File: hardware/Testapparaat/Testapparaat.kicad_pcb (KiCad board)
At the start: 2 copper layers, 102 parts, among them J1 MEM2051-00-195-00-A, J10 B-, J11 Display_shield, J2 Module_1, J3 Module_2, J4 DEBUG, J5 FPC_40P_LCD_ILI9488, J6 DB9_Female, J7 Emergency Stop Button, J8 CON-SOCJ-2155, J9 B+, Q1 BC817, Q2 BC817, Q3 BC817, Q4 IRFR9024N, Q5 IRFR9024N, Q6 IRFR9024N, SW1 RST, SW2 on/off switch, SW3 Menu, SW4 Back, SW5 RotaryEncoder_Switch, SW6 START, SW7 STOP, U1 74HC595 (SIPO Shift register), U2 ESP32-WROOM-32, U3 MAX232, U4 74AUC1G74, U5 TCA9534 (IO Expander), U6 74HC14

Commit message: -enh Made a start at pcb design
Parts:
- removed C6: 2.2u, Capacitor_SMD:C_0603_1608Metric_Pad1.08x0.95mm_HandSolder
- removed D8: 1N5401, Diode_THT:D_DO-201AD_P15.24mm_Horizontal
- removed D9: 1N4448, Diode_THT:D_DO-35_SOD27_P7.62mm_Horizontal
- removed PS1, PS2: LMR50410YFQDBVRQ1, LMR50410YFQDBVRQ1:SOT95P280X145-6N
- removed SW3: Menu, Button_Switch_SMD:SW_SPST_B3S-1000
- removed SW4: Back, Button_Switch_SMD:SW_SPST_B3S-1000
- removed SW5: RotaryEncoder_Switch, Rotary_Encoder:RotaryEncoder_Alps_EC11E-Switch_Vertical_H20mm_CircularMountingHoles
- removed SW6: START, Button_Switch_SMD:SW_SPST_B3S-1000
- removed SW7: STOP, Button_Switch_SMD:SW_SPST_B3S-1000
- removed U3: MAX232, Package_SO:SO-16_3.9x9.9mm_P1.27mm
- added C22: 100n, Capacitor_SMD:C_0603_1608Metric_Pad1.08x0.95mm_HandSolder, F.Cu at (71.8, 101.8)
- added J12: GPIO_INPUTS, Connector_PinHeader_2.54mm:PinHeader_1x04_P2.54mm_Horizontal, F.Cu at (99.4, -21.1)
- added J13: FrontPanel, Connector_PinHeader_2.54mm:PinHeader_2x08_P2.54mm_Vertical_SMD, F.Cu at (159.9, -9.95)
- added J14: GPIO_OUTPUT, Connector_PinHeader_2.54mm:PinHeader_2x04_P2.54mm_Vertical_SMD, F.Cu at (69.3, 6.75)
- added R38: 10k, Resistor_SMD:R_0603_1608Metric_Pad0.98x0.95mm_HandSolder, F.Cu at (123.5, -3.29)
- added R40: 10k, Resistor_SMD:R_0603_1608Metric_Pad0.98x0.95mm_HandSolder, F.Cu at (111.6, -3.85)
- added R41: 10k, Resistor_SMD:R_0603_1608Metric_Pad0.98x0.95mm_HandSolder, F.Cu at (112.5, 0.90)
- added R42: 10k, Resistor_SMD:R_0603_1608Metric_Pad0.98x0.95mm_HandSolder, F.Cu at (168.8, -3.05)
- added R43: 10k, Resistor_SMD:R_0603_1608Metric_Pad0.98x0.95mm_HandSolder, F.Cu at (174.2, -9.40)
- added R44: 10k, Resistor_SMD:R_0603_1608Metric_Pad0.98x0.95mm_HandSolder, F.Cu at (167.9, 2.10)
- added U10: LM2596S-5, Package_TO_SOT_SMD:TO-263-5_TabPin3, F.Cu at (179.3, 137.6)
- added U11: LM2596S-3.3, Package_TO_SOT_SMD:TO-263-5_TabPin3, F.Cu at (197.0, 137.6)
- added U12: 74AUC1G74, Package_SO:VSSOP-8_2.3x2mm_P0.5mm, F.Cu at (98.2, -11.9)
- added U7: TCA9534 (IO Expander), TCA9534:SOP65P640X120-16N, F.Cu at (106.7, 2.20)
- added U8: 74HC14, Package_SO:SO-14_3.9x8.65mm_P1.27mm, F.Cu at (120.7, -14.4)
- added U9: 74HC14, Package_SO:SO-14_3.9x8.65mm_P1.27mm, F.Cu at (107.0, -14.7)
- C1, J4, Q1, Q2, R4, R5: moved to B.Cu
- C10, C11, C12, C13: value 0.1u -> 100n
- C14, C15, C16, C17, C18, C19, C20: value 1u -> 100n
- C4, C5: value 100n -> 1u
- C7: value 2.2u -> 1u
- C8, C9: value 10u -> 220u; footprint Capacitor_SMD:C_0603_1608Metric_Pad1.08x0.95mm_HandSolder -> Capacitor_THT:C_Radial_D10.0mm_H12.5mm_P5.00mm
- D1, D2, D4: value 1N4448 -> SS310; footprint Diode_THT:D_DO-35_SOD27_P7.62mm_Horizontal -> Diode_SMD:D_SMA_Handsoldering
- D3, D5, D6, D7: value 1N4448 -> 1N4448WS; footprint Diode_THT:D_DO-35_SOD27_P7.62mm_Horizontal -> Diode_SMD:D_SOD-323
- J1: value MEM2051-00-195-00-A -> IO_SD; footprint MEM2051:MEM20510019500A -> Connector_PinHeader_2.54mm:PinHeader_1x06_P2.54mm_Horizontal
- J6: value DB9_Female -> IO_UART; footprint G17C0900132EU:G17C0900132EU -> Connector_PinHeader_2.54mm:PinHeader_1x04_P2.54mm_Horizontal
- L1: value 4.7uH -> 68uH
- L2: value 3.3uH -> 68uH
- R1: value 10k -> 1k
- R10: value 20k -> 1k
- R14, R15, R16, R17, R18, R2, R21, R22, R23, R24, R25, R26, R27, R28, R29, R34, R35: value 10k -> 22k
- R36, R37: value 10k -> 100k
- R7: value 91k -> 680
- R8: value 22k -> 220
- R9: value 43k -> 1,6k
- U4: value 74AUC1G74 -> 74HC595 (SIPO Shift register); footprint Package_SO:VSSOP-8_2.3x2mm_P0.5mm -> 74HC595D-Q100,118:74HC595DQ100118
- moved J3 166.4 mm to (253.8, 94.5)
- moved J6 160.1 mm to (58.3, 54.0), turned to 180 degrees
- moved R12 155.0 mm to (74.4, 108.5), turned to 180 degrees
- moved J11 152.6 mm to (63.6, 115.3)
- moved C4 152.4 mm to (101.4, -12.8), turned to -90 degrees
- moved R11 151.0 mm to (74.4, 109.9), turned to 180 degrees
- moved J5 149.4 mm to (90.2, 114.8), turned to 90 degrees
- moved J8 145.9 mm to (60.6, 160.7)
- moved J2 138.9 mm to (253.4, 47.5)
- moved R13 135.1 mm to (74.4, 107.0), turned to 180 degrees
- moved C13 134.6 mm to (63.9, 86.0), turned to 180 degrees
- moved J7 129.1 mm to (257.1, 20.0)
- moved R37 125.3 mm to (67.8, 87.5)
- moved C11 123.4 mm to (113.5, -7.95)
- moved SW2 122.2 mm to (65.2, 177.1), turned to 90 degrees
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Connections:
- C10 pad 1: Net-(C10-Pad1) -> +3.3V
- C10 pad 2: Net-(C10-Pad2) -> GND
- C11 pad 1: Net-(C11-Pad1) -> +3.3V
- C11 pad 2: Net-(C11-Pad2) -> GND
- C12 pad 1: GND -> +3.3V
- C12 pad 2: Net-(C12-Pad2) -> GND
- C13 pad 1: Net-(C13-Pad1) -> +3.3V
- C14 pad 1: MENU_BTN -> +3.3V
- C15 pad 1: BACK_BTN -> +3.3V
- C16 pad 1: Net-(C16-Pad1) -> +3.3V
- C17 pad 1: Net-(C17-Pad1) -> +3.3V
- C18 pad 1: Net-(C18-Pad1) -> GND
- C18 pad 2: GND -> +3.3V
- C19 pad 1: Net-(C19-Pad1) -> GND
- C19 pad 2: GND -> +3.3V
- C20 pad 1: Net-(C20-Pad1) -> +3.3V
- C4 pad 1: Net-(C4-Pad1) -> Net-(R35-Pad2)
- C4 pad 2: Net-(C4-Pad2) -> GND
- C5 pad 1: Net-(C5-Pad1) -> Net-(R29-Pad2)
- C5 pad 2: Net-(C5-Pad2) -> GND
- C7 pad 1: +BATT -> Net-(R34-Pad2)
- D1 pad 1: MENU_BTN -> Net-(D1-Pad1)
- D1 pad 2: Net-(D1-Pad2) -> GND
- D2 pad 1: BACK_BTN -> Net-(D2-Pad1)
- D2 pad 2: Net-(D2-Pad2) -> GND
- D3 pad 1: Net-(C16-Pad1) -> Net-(C21-Pad1)
- D3 pad 2: Net-(D3-Pad2) -> EMERGENCY_STOP_BTN
- D4 pad 1: Net-(C17-Pad1) -> +BATT
- D5 pad 1: Net-(C20-Pad1) -> Net-(R35-Pad2)
- D5 pad 2: Net-(D5-Pad2) -> Rotary_B_R
- D6 pad 1: Net-(C18-Pad1) -> Net-(R29-Pad2)
- D6 pad 2: Net-(D6-Pad2) -> Rotary_CLK_R
- D7 pad 1: Net-(C19-Pad1) -> Net-(R34-Pad2)
- D7 pad 2: Net-(D7-Pad2) -> Rotary_BTN_R
- J4 pad 5: /IO_port/TXD -> /MCU/GPIO_1/TXD0
- J4 pad 7: /IO_port/RXD -> /MCU/GPIO_3/RXD0
- J4 pad 9: DTS -> DTR
- J6 pad 1: unconnected-(J6-Pad1) -> +3.3V
- J6 pad 2: Net-(J6-Pad2) -> /MCU/GPIO_1/TXD0
- J6 pad 3: Net-(J6-Pad3) -> /MCU/GPIO_3/RXD0
- J6 pad 4: Net-(J6-Pad4) -> GND
- J7 pad 1: unconnected-(J7-Pad1) -> GND
- J7 pad 2: GND -> unconnected-(J7-Pad2)
- J8 pad 1: Net-(D8-Pad2) -> Net-(D4-Pad2)
- L1 pad 1: Net-(C4-Pad1) -> Net-(D1-Pad1)
- L2 pad 1: Net-(C5-Pad1) -> Net-(D2-Pad1)
- R1 pad 1: Net-(R1-Pad1) -> +3.3V
- R1 pad 2: +3.3V -> Net-(R1-Pad2)
- R14 pad 1: Net-(D1-Pad2) -> +3.3V
- R14 pad 2: GND -> BTN_4_R
- R15 pad 1: Net-(D2-Pad2) -> +3.3V
- R15 pad 2: GND -> BTN_5_R
- R16 pad 2: Net-(D5-Pad2) -> BTN_1_R
- R17 pad 2: Net-(D7-Pad2) -> BTN_2_R
- R18 pad 2: Net-(D6-Pad2) -> BTN_9_R
- R2 pad 2: Net-(R2-Pad2) -> BTN_3_R
- R21 pad 1: Net-(R21-Pad1) -> +3.3V
- R21 pad 2: +3.3V -> BTN_8_R
- R22 pad 1: Net-(D1-Pad2) -> +3.3V
- R22 pad 2: MENU_BTN -> BTN_10_R
- R23 pad 1: Net-(D2-Pad2) -> +3.3V
- R23 pad 2: BACK_BTN -> BTN_6_R
- R24 pad 1: Net-(D3-Pad2) -> +3.3V
- R24 pad 2: Net-(C16-Pad1) -> BTN_7_R
- R25 pad 1: Net-(D4-Pad2) -> +3.3V
- R25 pad 2: Net-(C17-Pad1) -> Net-(R25-Pad2)
- R26 pad 1: Net-(D4-Pad2) -> +3.3V
- R26 pad 2: +3.3V -> GPIO_INPUT_1_R
- R27 pad 1: Net-(C20-Pad1) -> +3.3V
- R27 pad 2: Net-(D5-Pad2) -> GPIO_INPUT_2_R
- R28 pad 1: Net-(D6-Pad2) -> +3.3V
- R28 pad 2: Net-(C18-Pad1) -> Net-(R28-Pad2)
- R29 pad 1: Net-(D7-Pad2) -> +3.3V
- R29 pad 2: Net-(C19-Pad1) -> Net-(R29-Pad2)
- R34 pad 2: SPI_CLK -> Net-(R34-Pad2)
- R35 pad 2: SPI_MOSI -> Net-(R35-Pad2)
- R36 pad 1: +3.3V -> /MCU/SENSOR_VN/GPIO_IN_39
- R36 pad 2: SD_CS -> ID_MOD_2
- R37 pad 1: +3.3V -> /MCU/SENSOR_VP/GPIO_IN_36
- R37 pad 2: SPI_MISO -> ID_MOD_1
- U1 pad 13: GND -> OE
- U1 pad 9: unconnected-(U1-Pad9) -> Net-(U1-Pad9)
- U2 pad 10: IO_EXP_INT -> OE
- U2 pad 11: Rotary_CLK -> RCLK
- U2 pad 12: Rotary_DT -> SRCLK
- U2 pad 34: /IO_port/RXD -> /MCU/GPIO_3/RXD0
- U2 pad 35: /IO_port/TXD -> /MCU/GPIO_1/TXD0
- U2 pad 4: ID_MOD_2 -> /MCU/SENSOR_VP/GPIO_IN_36
- U2 pad 5: ID_MOD_1 -> /MCU/SENSOR_VN/GPIO_IN_39
- U2 pad 6: SRCLK -> Rotary_DT
- U2 pad 7: SER -> IO_EXP_INT
- U2 pad 8: EMERGENCY_STOP_BTN -> SER
- U2 pad 9: RCLK -> Rotary_CLK
- U4 pad 1: Rotary_CLK -> GPIO_OUTPUT_2
- U4 pad 2: Rotary_B -> GPIO_OUTPUT_3
- U4 pad 3: unconnected-(U4-Pad3) -> GPIO_OUTPUT_4
- U4 pad 4: GND -> GPIO_OUTPUT_5
- U4 pad 5: Rotary_DT -> GPIO_OUTPUT_6
- U4 pad 6: +3.3V -> GPIO_OUTPUT_7
- U4 pad 7: +3.3V -> GPIO_OUTPUT_8
- U4 pad 8: +3.3V -> GND
- U5 pad 10: BACK_BTN -> BTN_2
- U5 pad 11: ENCODER_BTN -> BTN_3
- U5 pad 12: MOD_PSU_EN -> BTN_4
- U5 pad 6: START_BTN -> EMERGENCY_STOP_BTN
- U5 pad 7: STOP_BTN -> Rotary_BTN
- U5 pad 9: MENU_BTN -> BTN_1
- U6 pad 10: STOP_BTN -> BTN_4
- U6 pad 11: Net-(C19-Pad1) -> BTN_4_R
- U6 pad 12: ENCODER_BTN -> BTN_5
- U6 pad 13: Net-(C20-Pad1) -> BTN_5_R
- U6 pad 3: Net-(C17-Pad1) -> BTN_1_R
- U6 pad 4: Rotary_B -> BTN_1
- U6 pad 5: Net-(C16-Pad1) -> BTN_2_R
- U6 pad 6: Rotary_CLK -> BTN_2
- U6 pad 8: START_BTN -> BTN_3
- U6 pad 9: Net-(C18-Pad1) -> BTN_3_R

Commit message: -add Layout zo goed als af
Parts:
- C12, C13, C2, C3, C8, C9, D1, D2, J6, L1, L2, R10, R3, R36, R37, R6, R7, R8, R9, SW1, U10, U11, U2: moved to B.Cu
- moved J12 194.9 mm to (220.5, 131.6), turned to -90 degrees
- moved U1 194.5 mm to (239.8, 106.2)
- moved C15 192.2 mm to (247.8, 78.6)
- moved R1 192.2 mm to (240.0, 78.3)
- moved U4 192.2 mm to (237.7, 84.9)
- moved C16 192.2 mm to (234.2, 77.7)
- moved J14 190.5 mm to (238.1, 95.0)
- moved R20 184.6 mm to (230.6, 100.6), turned to -90 degrees
- moved R34 181.9 mm to (214.9, 124.0)
- moved C11 181.4 mm to (233.4, 128.3)
- moved R18 181.4 mm to (246.4, 124.3)
- moved R23 181.4 mm to (238.4, 114.8)
- moved R25 181.4 mm to (246.4, 118.4)
- moved R26 181.4 mm to (233.4, 124.1)
- moved R27 181.4 mm to (233.0, 121.7)
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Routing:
- net Net-(Q3-Pad1): track 0.00 -> 4.76 mm
- net GND: track 0.00 -> 4.76 mm
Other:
- board outline added: 141.6 x 97.8 mm

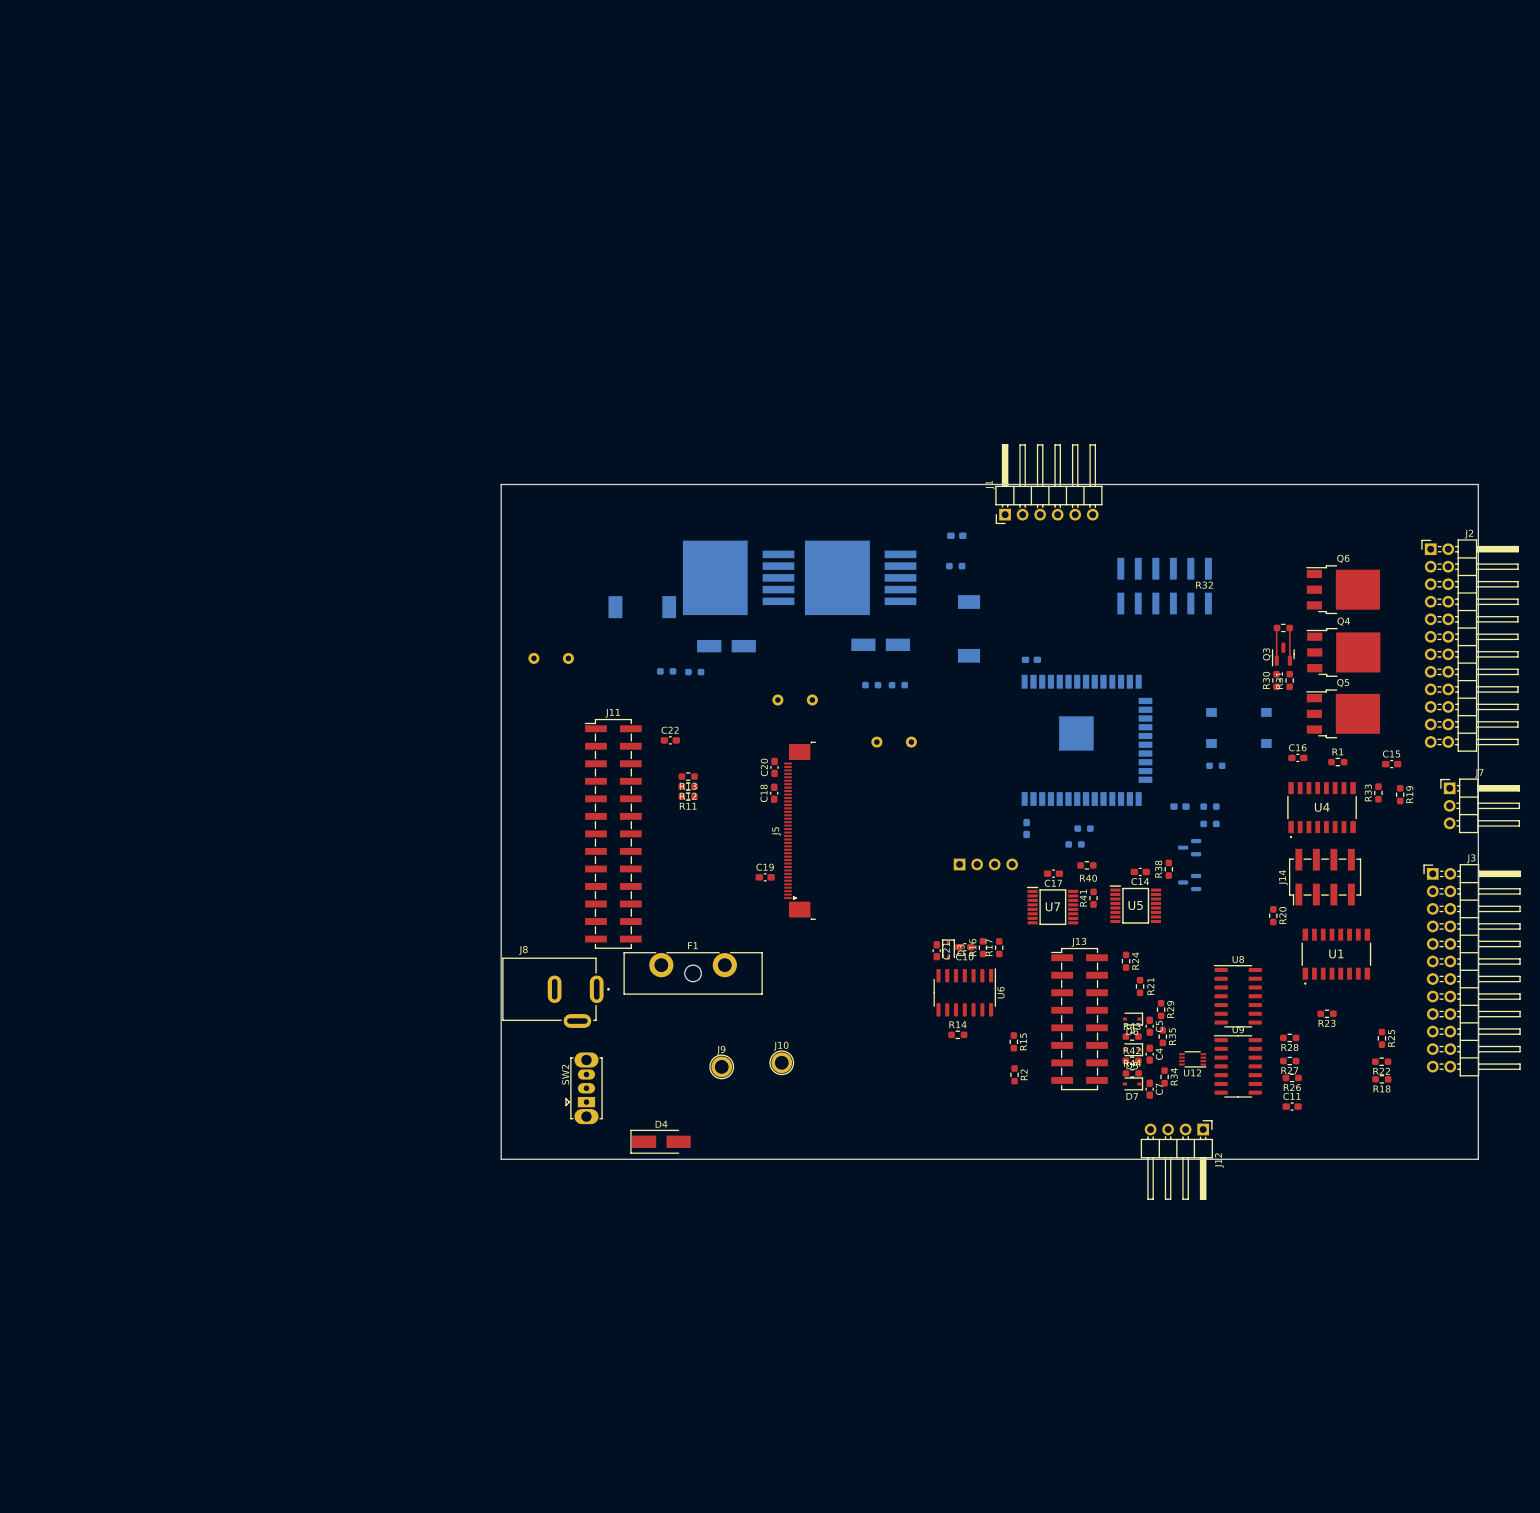
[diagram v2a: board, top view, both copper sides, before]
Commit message: -enh PCB routed power section
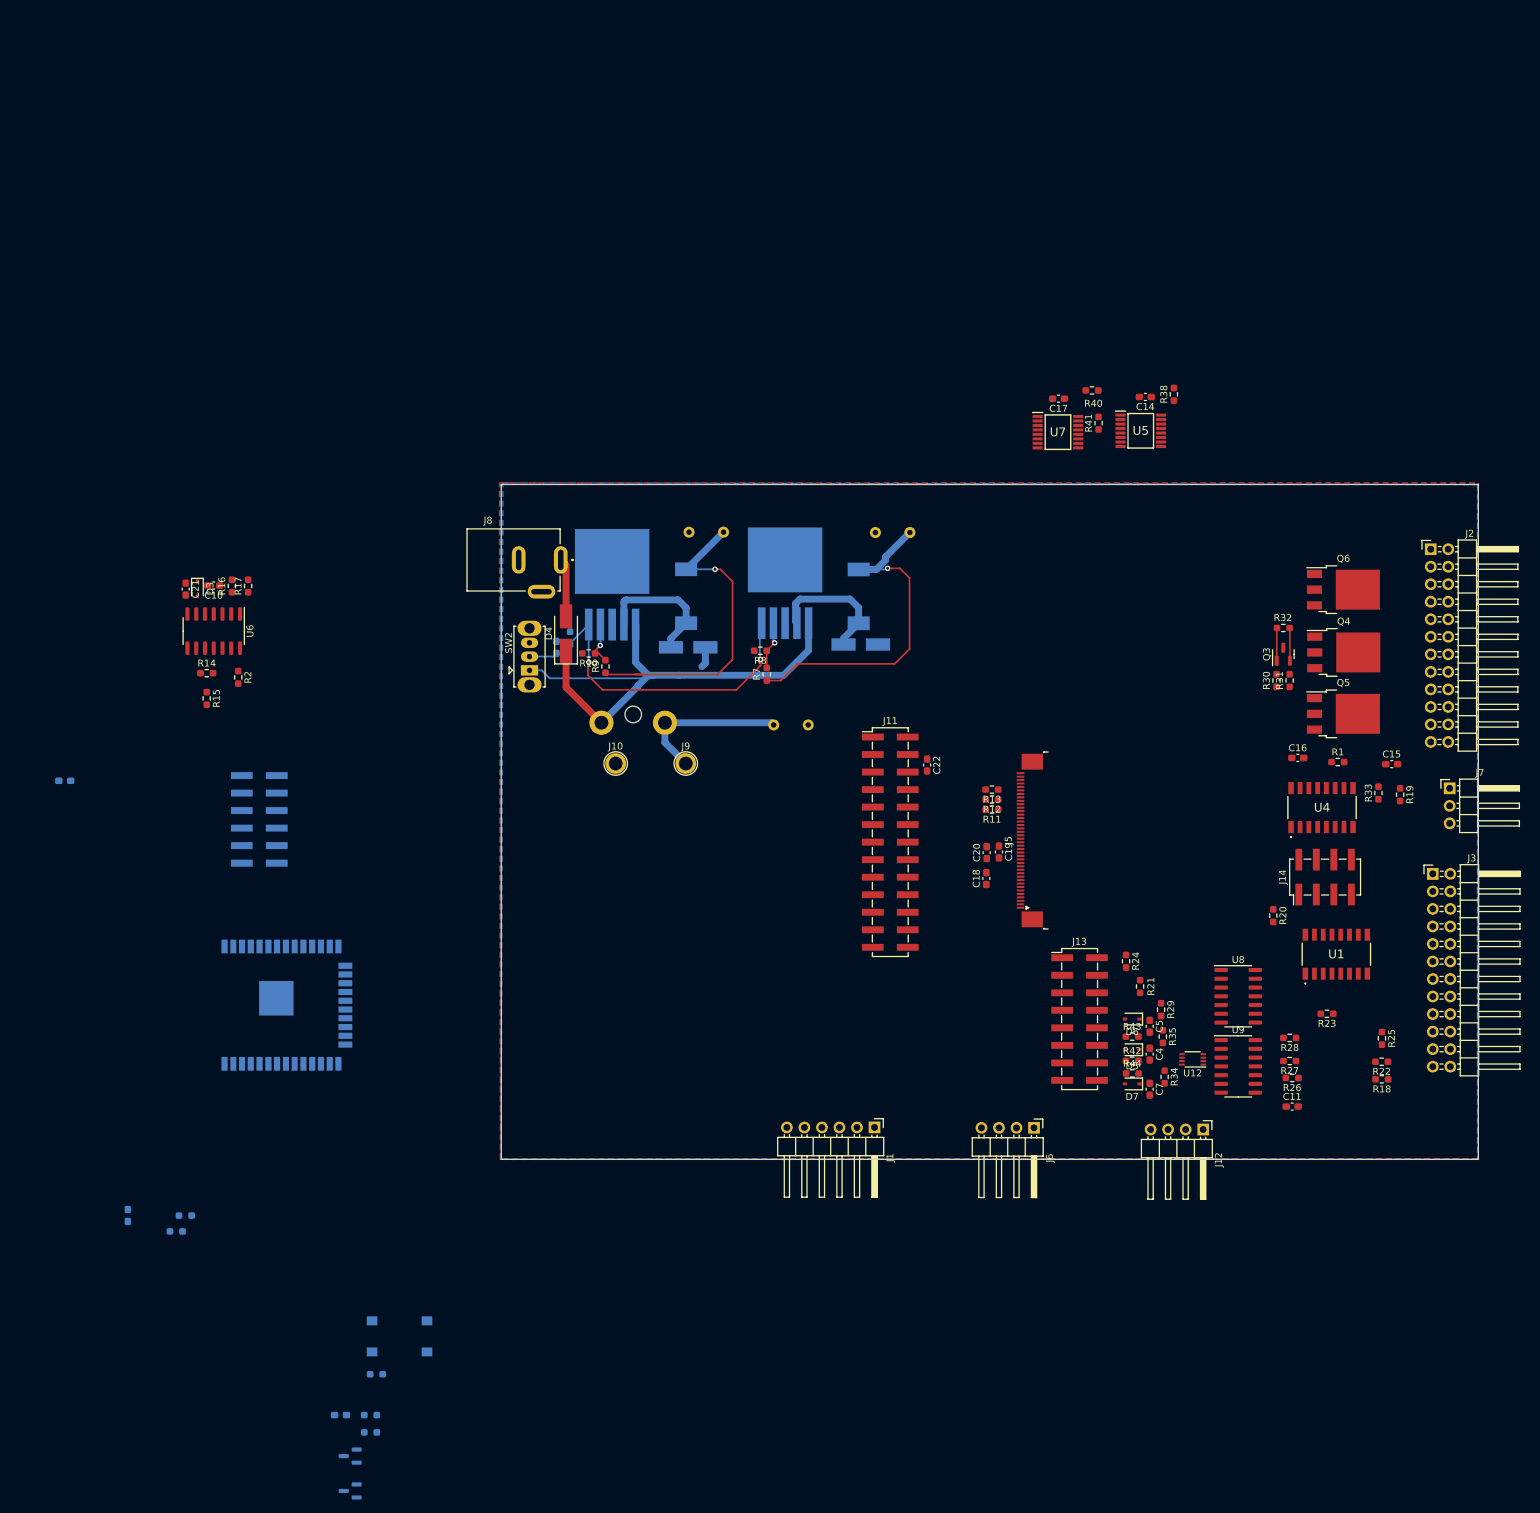
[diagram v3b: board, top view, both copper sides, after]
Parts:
- F1: moved to B.Cu
- J6, R10, R7, R8, R9: moved to F.Cu
- moved R3 150.2 mm to (100.7, 167.0)
- moved C1 150.2 mm to (95.5, 173.0)
- moved Q1 150.2 mm to (96.9, 184.0)
- moved Q2 150.2 mm to (96.9, 178.9)
- moved R4 150.2 mm to (99.8, 175.5)
- moved R5 150.2 mm to (99.8, 173.0)
- moved SW1 150.2 mm to (104.0, 161.6)
- moved C13 141.8 mm to (64.6, 144.0)
- moved R37 141.8 mm to (71.7, 146.3)
- moved R36 141.8 mm to (73.0, 144.0)
- moved C12 141.2 mm to (55.5, 81.0)
- moved J4 135.5 mm to (83.7, 86.6), turned to 0 degrees
- moved R15 127.1 mm to (76.1, 69.1)
- moved R2 126.4 mm to (80.6, 66.1)
- moved U2 122.1 mm to (86.9, 113.6)
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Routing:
- net +BATT: track 0.00 -> 77.7 mm
- net +5V: track 0.00 -> 50.9 mm, vias 0 -> 1
- net REG_EN: track 0.00 -> 50.2 mm, vias 0 -> 2
- net +3.3V: track 0.00 -> 47.2 mm, vias 0 -> 1
- net Net-(C2-Pad1): track 0.00 -> 23.5 mm
- net Net-(D2-Pad1): track 0.00 -> 19.5 mm
- net Net-(D1-Pad1): track 0.00 -> 19.1 mm
- net Net-(D4-Pad2): track 0.00 -> 8.48 mm
- net Net-(R7-Pad2): track 0.00 -> 7.62 mm, vias 0 -> 1
- net Net-(R10-Pad1): track 0.00 -> 6.44 mm, vias 0 -> 1
- net GND: track 4.76 -> 7.77 mm
- added copper zone on B.Cu, net GND
- added copper zone on F.Cu, net GND

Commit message: -enh First look at layout, proposed it to the team
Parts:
- C14, C17, R38, R40, R41, U5, U7: moved to B.Cu
- C2, C8, C9: moved to F.Cu
- F1: footprint Fuse:Fuseholder_Blade_ATO_Littelfuse_Pudenz_2_Pin -> Fuse:Fuseholder_Littelfuse_100_series_5x20mm
- L1, L2: footprint Inductor_SMD:L_Bourns-SRU8028_8.0x8.0mm -> srr1260:SRR1260-680M
- moved C12 166.0 mm to (221.2, 71.0)
- moved J4 158.5 mm to (242.0, 81.1)
- moved C13 156.0 mm to (200.5, 67.5)
- moved R36 156.0 mm to (208.9, 67.5)
- moved R37 156.0 mm to (207.5, 69.8)
- moved U2 139.2 mm to (223.8, 88.8)
- moved R4 126.2 mm to (192.7, 90.2)
- moved C1 126.2 mm to (188.4, 87.6)
- moved Q1 126.2 mm to (189.8, 98.6)
- moved Q2 126.2 mm to (189.8, 93.6)
- moved R3 126.2 mm to (193.6, 81.7)
- moved R5 126.2 mm to (192.7, 87.6)
- moved SW1 126.2 mm to (196.9, 76.3)
- moved C10 122.6 mm to (192.6, 93.8)
- moved D3 122.6 mm to (190.2, 94.3)
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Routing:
- net Net-(C2-Pad1): track 23.5 -> 0.46 mm
- net +3.3V: track 47.2 -> 39.6 mm
- net +5V: track 50.9 -> 45.4 mm
- removed copper zone on B.Cu, net GND
- removed copper zone on F.Cu, net GND
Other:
- board size 141.6 x 97.8 mm -> 138.9 x 89.6 mm
- board text added: "Display"

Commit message: -enh change slave address of second io expander
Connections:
- U7 pad 1: GND -> +3.3V
